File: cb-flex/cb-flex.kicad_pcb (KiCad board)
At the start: 4 copper layers, 50.1 x 70.1 mm, 35 parts, among them P1 CONN_01X14, P2 CONN_01X14, P3 CONN_01X02, P4 CONN_01X01, SW1 SW_PUSH, U1 BMP180, U2 MAX1724, U3 SI7021, U4 TSL2561

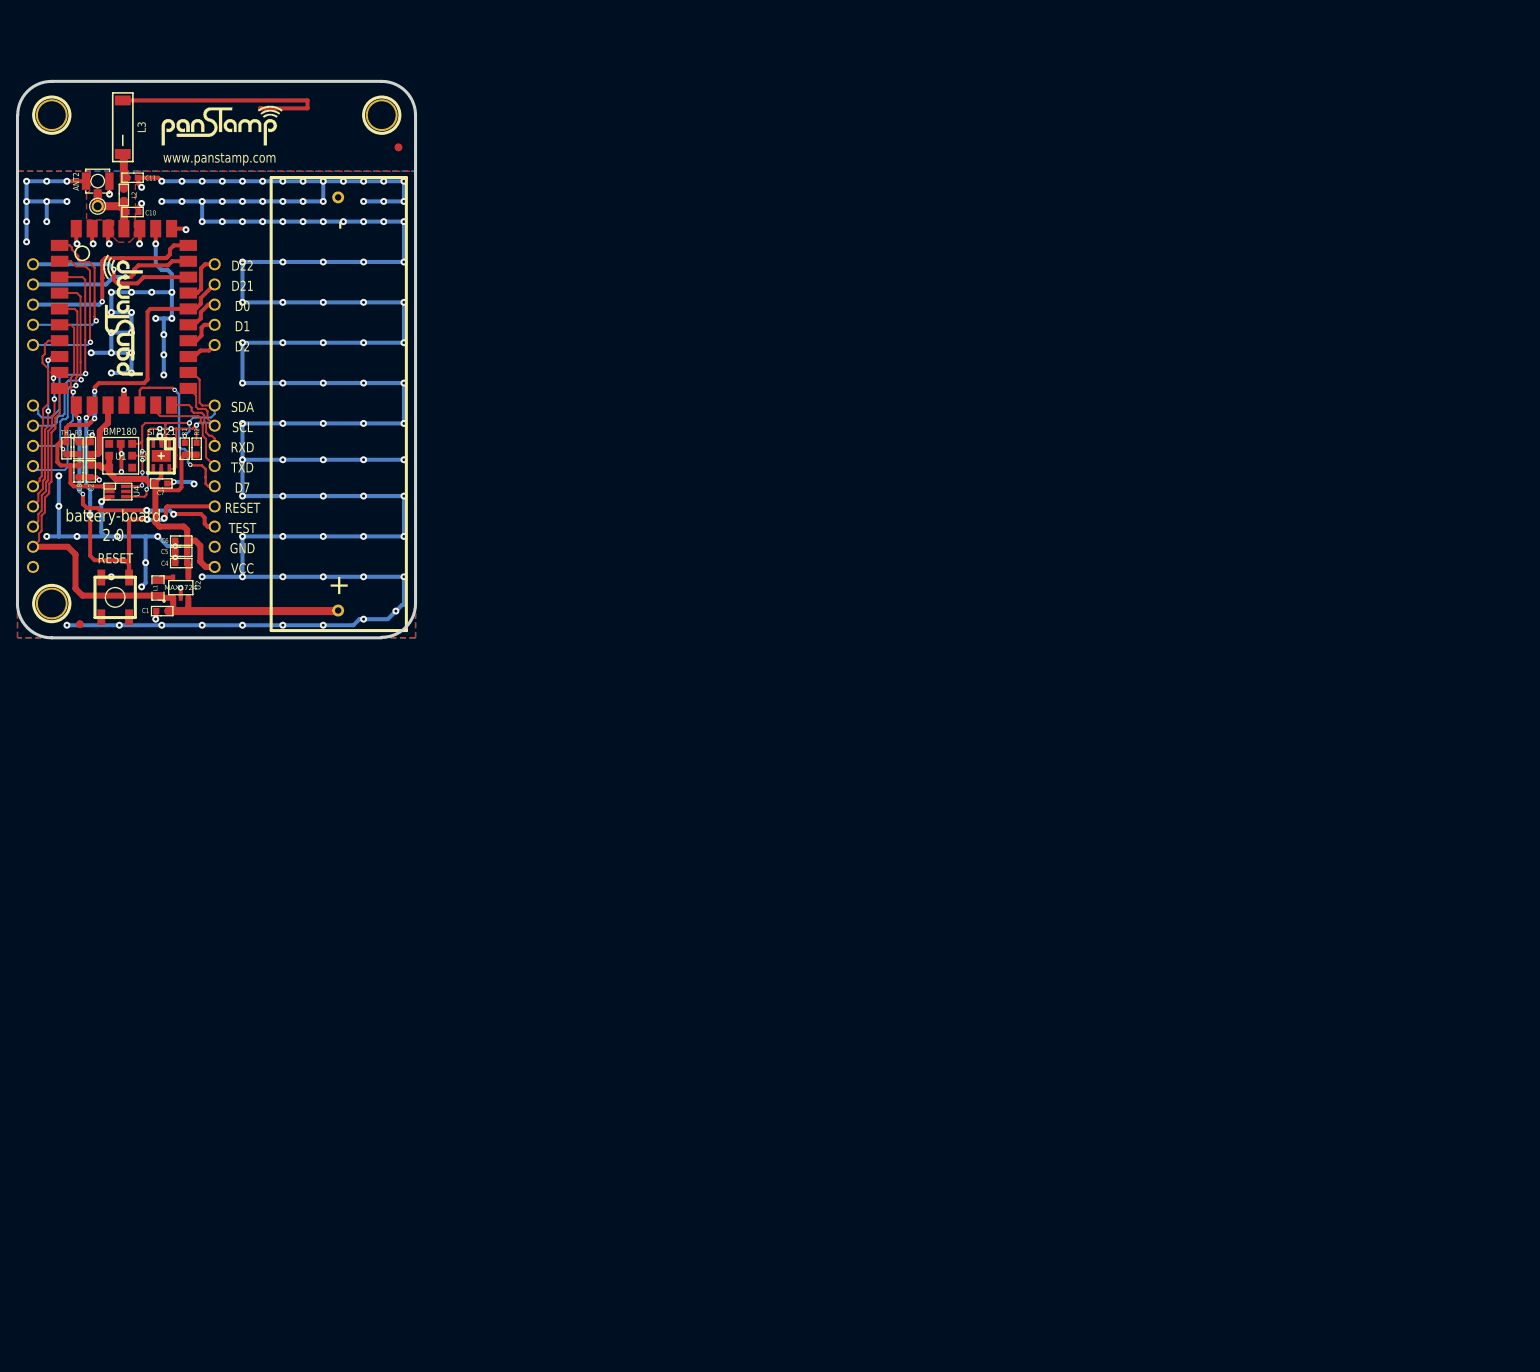
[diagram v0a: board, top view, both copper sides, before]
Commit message: Finishing schematic and starting PCB layout
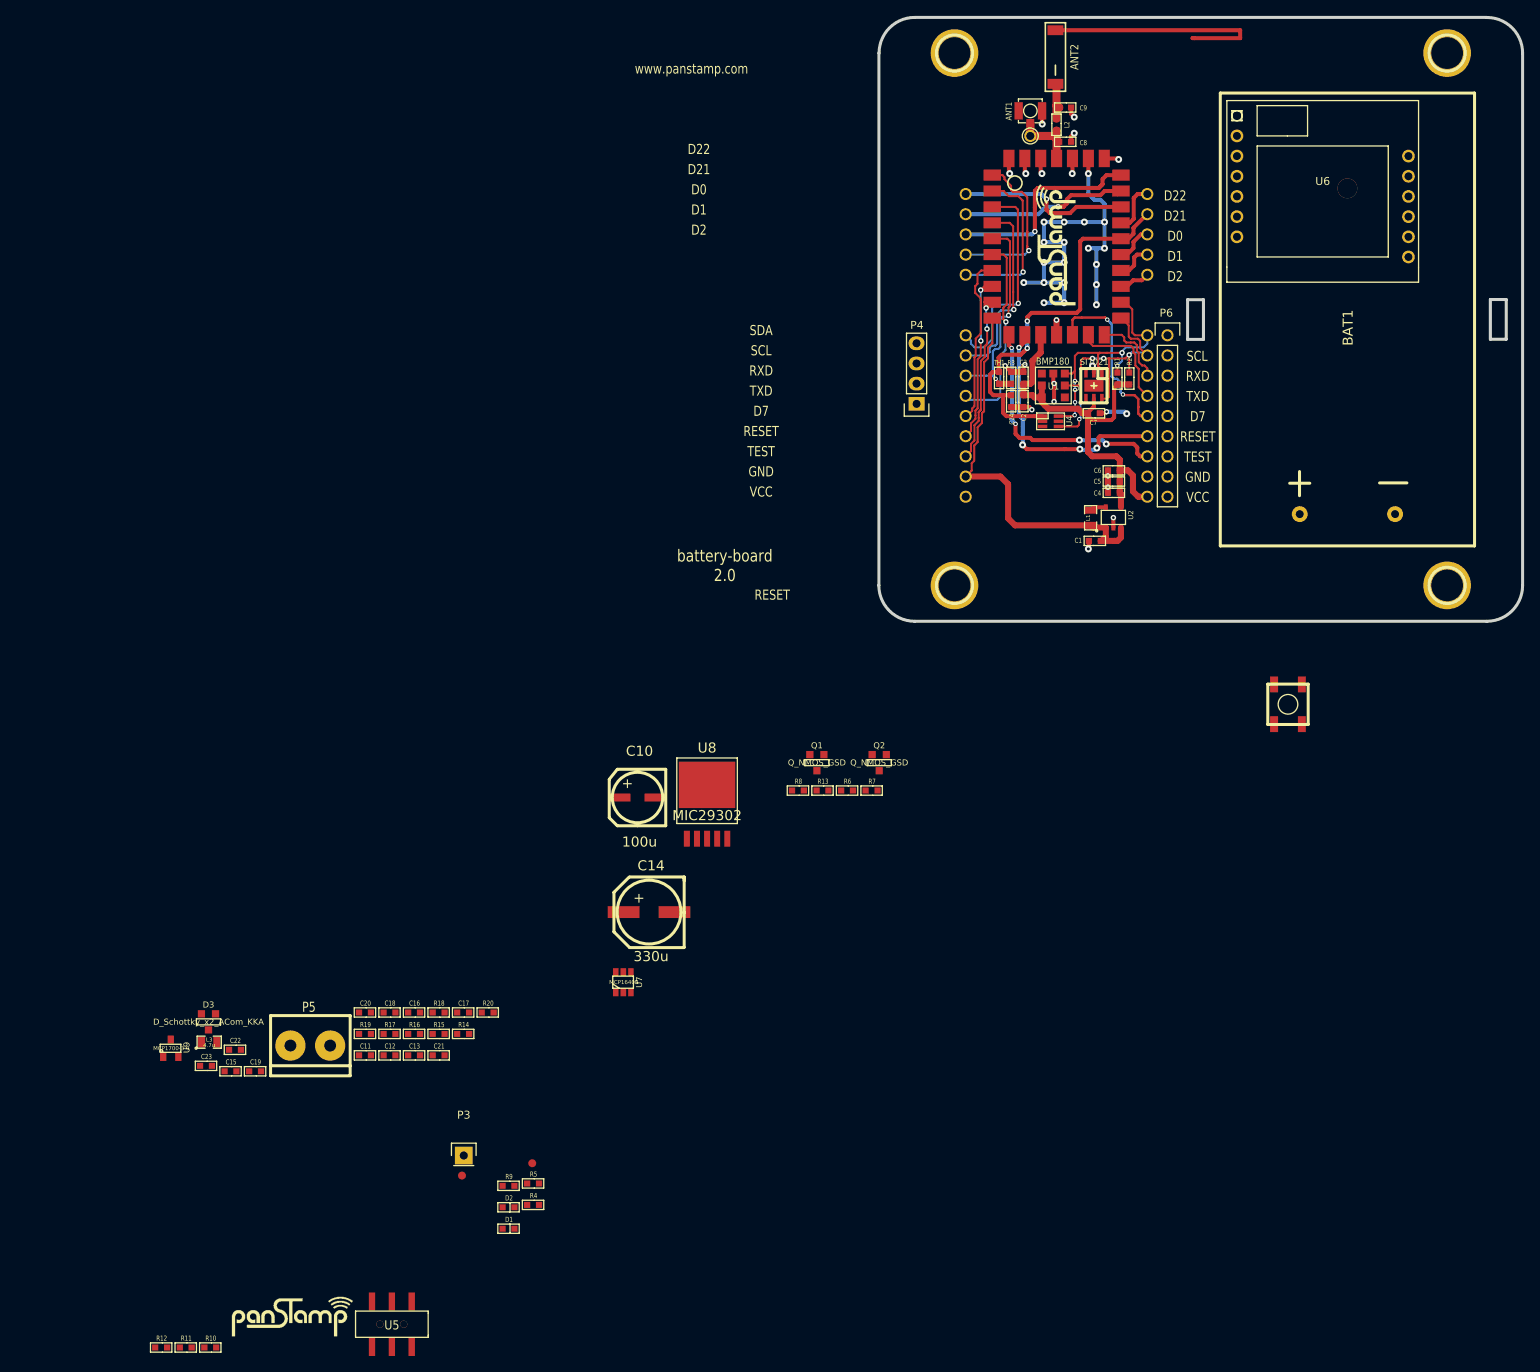
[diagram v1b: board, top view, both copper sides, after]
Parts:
- removed the 1PIN at (88.8, 38.4)
- removed the 1PIN at (130.3, 38.4)
- removed the 1PIN at (88.8, 99.9)
- added 1PIN: P***, 1pin, F.Cu at (264.4, 30.6)
- added 1PIN: P***, 1pin, F.Cu at (202.4, 30.6)
- added 1PIN: P***, 1pin, F.Cu at (202.4, 97.6)
- added 1PIN: P***, 1pin, F.Cu at (264.4, 97.6)
- added BAT1: CONN_2, mymods:BAT_AA_HOLDER_02, F.Cu at (251.8, 88.6)
- added C10: 100u, mysmd:SMDCPOL_6.3, F.Cu at (162.5, 124.3)
- added C11: 10u, mysmd:SM0603S, F.Cu at (128.2, 156.8)
- added C12: 1u, mysmd:SM0603S, F.Cu at (131.3, 156.8)
- added C13: 10u, mysmd:SM0603S, F.Cu at (134.4, 156.8)
- added C14: 330u, mysmd:SMDCPOL_8, F.Cu at (163.9, 138.7)
- added C15: 1u, mysmd:SM0603S, F.Cu at (111.3, 158.8)
- added C16: 1u, mysmd:SM0603S, F.Cu at (134.4, 151.4)
- added C17: 100n, mysmd:SM0603S, F.Cu at (140.5, 151.4)
- added C18: 100n, mysmd:SM0603S, F.Cu at (131.3, 151.4)
- added C19: 10u, old_mysmd:SM0603S, F.Cu at (114.4, 158.8)
- added C20: 1u, mysmd:SM0603S, F.Cu at (128.2, 151.4)
- added C21: 10u, mysmd:SM0603S, F.Cu at (137.5, 156.8)
- added C22: 1u, mysmd:SM0603S, F.Cu at (111.8, 156.1)
- added C23: 100n, old_mysmd:SM0603S, F.Cu at (108.2, 158.1)
- added D1: LED, mysmd:SM0603S_POL, F.Cu at (146.3, 178.6)
- added D2: LED, mysmd:SM0603S_POL, F.Cu at (146.3, 175.9)
- added D3: D_Schottky_x2_ACom_KKA, mysmd:SOT23, F.Cu at (108.5, 152.5)
- added L3: 4.7u, libcms:SM0805, F.Cu at (108.6, 155.1)
- added P4: CONN_01X04, Pin_Headers:Pin_Header_Straight_1x04, F.Cu at (197.6, 74.8)
- added P5: CONN_01X02, myconnectors:terminal_block_5mm_2P, F.Cu at (121.3, 155.5)
- added P6: CONN_01X09, Pin_Headers:Pin_Header_Straight_1x09, F.Cu at (229.2, 66.1)
- added Q1: Q_NMOS_GSD, mysmd:SOT23, F.Cu at (185.1, 119.9)
- added Q2: Q_NMOS_GSD, mysmd:SOT23, F.Cu at (192.9, 119.9)
- added R10: 1k, mysmd:SM0603S, F.Cu at (108.7, 193.5)
- added R11: 1k, mysmd:SM0603S, F.Cu at (105.6, 193.5)
- added R12: 1k, mysmd:SM0603S, F.Cu at (102.5, 193.5)
- added R13: 10k, mysmd:SM0603S, F.Cu at (185.8, 123.4)
- added R14: 976k, mysmd:SM0603S, F.Cu at (140.5, 154.1)
- added R15: 309k, mysmd:SM0603S, F.Cu at (137.5, 154.1)
- added R16: 100k, mysmd:SM0603S, F.Cu at (134.4, 154.1)
- added R17: 43k, mysmd:SM0603S, F.Cu at (131.3, 154.1)
- added R18: 0, mysmd:SM0603S, F.Cu at (137.5, 151.4)
- added R19: 0, mysmd:SM0603S, F.Cu at (128.2, 154.1)
- added R20: 0, mysmd:SM0603S, F.Cu at (143.6, 151.4)
- added R4: 470, mysmd:SM0603S, F.Cu at (149.3, 175.6)
- added R5: 470, mysmd:SM0603S, F.Cu at (149.3, 172.9)
- added R6: 10k, mysmd:SM0603S, F.Cu at (188.9, 123.4)
- added R7: 10k, mysmd:SM0603S, F.Cu at (192.0, 123.4)
- added R8: 10k, mysmd:SM0603S, F.Cu at (182.7, 123.4)
- added R9: 1k, mysmd:SM0603S, F.Cu at (146.3, 173.2)
- added U5: LY-SK10, mysmd:LY-SK10, F.Cu at (131.6, 190.6)
- added U6: SIM800L_module, mymods:SIM800L_MODULE, F.Cu at (248.7, 48.0)
- added U7: MCP1640B, libcms:SOT23_6, F.Cu at (160.7, 147.5)
- added U8: MIC29302, mysmd:TO-252, F.Cu at (171.3, 129.5)
- added U9: MCP1700-3.0, libcms:SOT23, F.Cu at (103.7, 155.9)
- C8: renamed from C10; value 2.2p -> N.P.
- C9: renamed from C11; value N.P -> N.P.
- P3: value CONN_01X02 -> CONN_01X01; footprint 12BH311P -> Pin_Headers:Pin_Header_Straight_1x01
- P7: renamed from P4; value CONN_01X01 -> CONN_01X09
- SW1: value SW_PUSH -> SW_PUSH_SMALL
- TH1: value NTC -> THERMISTOR
- U2: value MAX1724 -> MAX1724-3.3
- moved www.panstamp.com 150.2 mm to (111.4, 186.8)
- moved SW1 148.2 mm to (244.4, 112.6)
- moved fiducial 129.0 mm to (149.2, 170.3)
- moved ANT1 117.7 mm to (211.9, 37.9)
- moved C1 117.7 mm to (220.1, 92.0)
- moved C3 117.7 mm to (211.1, 71.5)
- moved P1 117.7 mm to (203.8, 70.1)
- moved PS1 117.7 mm to (215.2, 55.0)
- moved R1 117.7 mm to (222.9, 71.6)
- moved U1 117.7 mm to (214.8, 72.4)
- moved U3 117.7 mm to (219.9, 72.5)
- moved U4 117.7 mm to (214.5, 76.9)
- moved C24 117.7 mm to (209.5, 74.4)
- moved C7 117.7 mm to (219.9, 75.9)
- moved C8 117.7 mm to (216.3, 41.8)
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- renumbered ANT2 to ANT1, L3 to ANT2, C8 to C24
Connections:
- net /A5 renamed A5
- net /CHIP_ANT renamed Net-(ANT2-Pad1)
- net /D14 renamed TRIG
- net /D15 renamed ECHO
- net /D21 renamed EN_EXTERNAL
- net /D22 renamed EN_SENSOR
- net /D5 renamed /RXD
- net /D6 renamed /SIM_RXD
- ANT1 pad 1: /TOANT -> Net-(ANT1-Pad1)
- C8 pad 1: /TOANT -> Net-(ANT1-Pad1)
- L2 pad 1: /TOANT -> Net-(ANT1-Pad1)
- P1 pad 13: +BATT -> BAT_ADC
- P2 pad 6: /I2C_SDA -> /SDA
- P2 pad 7: /I2C_SCL -> /SCL
- P3 pad 1: +BATT -> Net-(ANT1-Pad1)
- P7 pad 1: /TOANT -> /SDA
- PS1 pad 10: +BATT -> BAT_ADC
- PS1 pad 18: /I2C_SCL -> /SCL
- PS1 pad 19: /I2C_SDA -> /SDA
- PS1 pad 31: /TOANT -> Net-(ANT1-Pad1)
- R1 pad 2: /I2C_SDA -> SDA
- R2 pad 2: /I2C_SCL -> SCL
- U1 pad 5: /I2C_SCL -> SCL
- U1 pad 6: /I2C_SDA -> SDA
- U3 pad 1: /I2C_SDA -> SDA
- U3 pad 6: /I2C_SCL -> SCL
- U4 pad 4: /I2C_SCL -> SCL
- U4 pad 6: /I2C_SDA -> SDA
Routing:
- net GND: track 520.5 -> 88.0 mm, vias 150 -> 40
- net +BATT: track 72.4 -> 24.4 mm
- net /I2C_SCL: track 37.2 -> 0.00 mm, vias 5 -> 0
- net /I2C_SDA: track 34.6 -> 0.00 mm, vias 6 -> 0
- net /SDA: track 0.00 -> 32.5 mm, vias 0 -> 5
- net /SCL: track 0.00 -> 30.0 mm, vias 0 -> 5
- net BAT_ADC: track 0.00 -> 26.5 mm
- net /TOANT: track 14.6 -> 0.00 mm
- net /RESET: track 46.3 -> 32.1 mm
- net Net-(ANT1-Pad1): track 0.00 -> 10.1 mm
- net SCL: track 0.00 -> 7.22 mm
- net SDA: track 0.00 -> 6.66 mm, vias 0 -> 1
- removed copper zone on B.Cu, net GND
- removed copper zone on F.Cu, net GND
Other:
- board size 50.1 x 70.1 mm -> 81 x 76 mm
- net class Default: clearance 0.127 -> 0.1778; trace_width 0.1524 -> 0.2032; via_dia 0.5588 -> 1.016; via_drill 0.3048 -> 0.6096
- rule trace_clearance: 0.127 -> 0.1778

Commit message: Finishing layout
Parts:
- removed C23: 100n, old_mysmd:SM0603S
- removed the P3 at (140.6, 169.4)
- added C29: 100n, mysmd:SM0603S, F.Cu at (232.6, 56.7)
- added C31: 1u, mysmd:SM0603S, F.Cu at (230.3, 59.5)
- added C32: 100n, mysmd:SM0603S, F.Cu at (230.3, 54.3)
- added U10: MMA8652FC, mysmd:DFN-10, F.Cu at (230.2, 56.9)
- ?: renamed from www.panstamp.com; value Battery board V.2.0 -> (none)
- C21: value 10u -> 1u
- C22: value 1u -> 100n
- D1: footprint mysmd:SM0603S_POL -> SM0603S_POL
- P3: renamed from P7; value CONN_01X09 -> CONN_01X01
- U9: value MCP1700-3.0 -> AP7365-30; footprint libcms:SOT23 -> libcms:SOT23-5
- moved ? 205.4 mm to (241.2, 27.7)
- moved R12 193.8 mm to (240.8, 57.8), turned to 90 degrees
- moved R10 193.3 mm to (233.8, 46.2)
- moved R11 192.7 mm to (242.4, 57.8), turned to 90 degrees
- moved fiducial 185.0 mm to (270.5, 30.6)
- moved U5 166.9 mm to (240.4, 64.0)
- moved D1 160.4 mm to (230.2, 41.9), turned to 90 degrees
- moved R4 158.8 mm to (230.2, 38.9), turned to 270 degrees
- moved R9 158.5 mm to (233.8, 41.0)
- moved D2 156.8 mm to (227.8, 41.9), turned to 90 degrees
- moved U9 156.8 mm to (239.4, 77.2), turned to 90 degrees
- moved R5 155.2 mm to (227.8, 38.9), turned to 270 degrees
- moved C19 151.6 mm to (239.4, 73.0), turned to 180 degrees
- moved C18 149.5 mm to (256.7, 70.0)
- moved D3 148.0 mm to (244.7, 94.7), turned to 270 degrees
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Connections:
- net /D0 renamed EN_ACC
- D1 pad 2: EN_SENSOR -> /D22
- D2 pad 2: EN_EXTERNAL -> /D21
- P1 pad 1: /D20 -> EN_SENSOR
- P1 pad 13: BAT_ADC -> +BATT
- P1 pad 5: /D16 -> EN_EXTERNAL
- P2 pad 1: EN_EXTERNAL -> /D21
- P2 pad 2: EN_SENSOR -> /D22
- P2 pad 4: /D1 -> ACC_INT1
- P2 pad 5: /D2 -> ACC_INT2
- P2 pad 6: /SDA -> SDA
- P2 pad 7: /SCL -> SCL
- P2 pad 9: /SIM_RXD -> /TXD
- P3 pad 1: /SDA -> Net-(ANT1-Pad1)
- P6 pad 1: /SDA -> SDA
- P6 pad 2: /SCL -> SCL
- P6 pad 4: /SIM_RXD -> /TXD
- PS1 pad 10: BAT_ADC -> +BATT
- PS1 pad 16: /SIM_RXD -> /TXD
- PS1 pad 18: /SCL -> SCL
- PS1 pad 19: /SDA -> SDA
- PS1 pad 2: /D16 -> EN_EXTERNAL
- PS1 pad 20: /D2 -> ACC_INT2
- PS1 pad 21: /D1 -> ACC_INT1
- PS1 pad 23: EN_SENSOR -> /D22
- PS1 pad 24: EN_EXTERNAL -> /D21
- PS1 pad 25: /D20 -> EN_SENSOR
- R10 pad 1: /D4 -> ACC_INT2
- R12 pad 1: /RXD -> /SIM_TXD
- R9 pad 1: /D3 -> ACC_INT1
- U5 pad 1: /PS_TXD -> /TXD
- U5 pad 5: /RXD -> /SIM_TXD
- U5 pad 6: /PS_RXD -> /RXD
- U9 pad 1: GND -> VAA
- U9 pad 2: VCC -> GND
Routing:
- net VAA: track 0.00 -> 103.5 mm
- net +BATT: track 24.4 -> 94.0 mm, vias 0 -> 2
- net GND: track 88.0 -> 136.2 mm, vias 40 -> 64
- net SCL: track 7.22 -> 53.9 mm, vias 0 -> 7
- net SDA: track 6.66 -> 48.9 mm, vias 1 -> 6
- net VDD: track 0.00 -> 39.7 mm, vias 0 -> 2
- net EN_EXTERNAL: track 6.36 -> 40.4 mm, vias 0 -> 1
- net /SDA: track 32.5 -> 0.00 mm, vias 5 -> 0
- net /TXD: track 0.00 -> 32.4 mm
- net Net-(C10-Pad1): track 0.00 -> 32.2 mm
- net ACC_INT2: track 0.00 -> 30.9 mm, vias 0 -> 3
- net /SCL: track 30.0 -> 0.00 mm, vias 5 -> 0
- net ACC_INT1: track 0.00 -> 29.5 mm, vias 0 -> 3
- net EN_SENSOR: track 49.7 -> 77.2 mm, vias 2 -> 3
- net BAT_ADC: track 26.5 -> 0.00 mm
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- added copper zone on B.Cu, net GND
- added copper zone on F.Cu, net GND
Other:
- net class Default: clearance 0.1778 -> 0.127; trace_width 0.2032 -> 0.1524; via_dia 1.016 -> 0.5588; via_drill 0.6096 -> 0.3048
- rule trace_clearance: 0.1778 -> 0.127
- board text added: "+5V"
- board text added: "flex-board 1.0"
- board text removed: "battery-board 2.0"
